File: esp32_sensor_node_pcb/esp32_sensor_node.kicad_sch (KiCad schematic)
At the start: 28 parts, among them J1 Conn_02x10_Odd_Even, Q1 2N7002K, SW1 SW_DIP_x01, SW2 SW_DIP_x01, U1 HT7833, U2 ESP32-WROOM-E, U3 MAX3483AEASA+

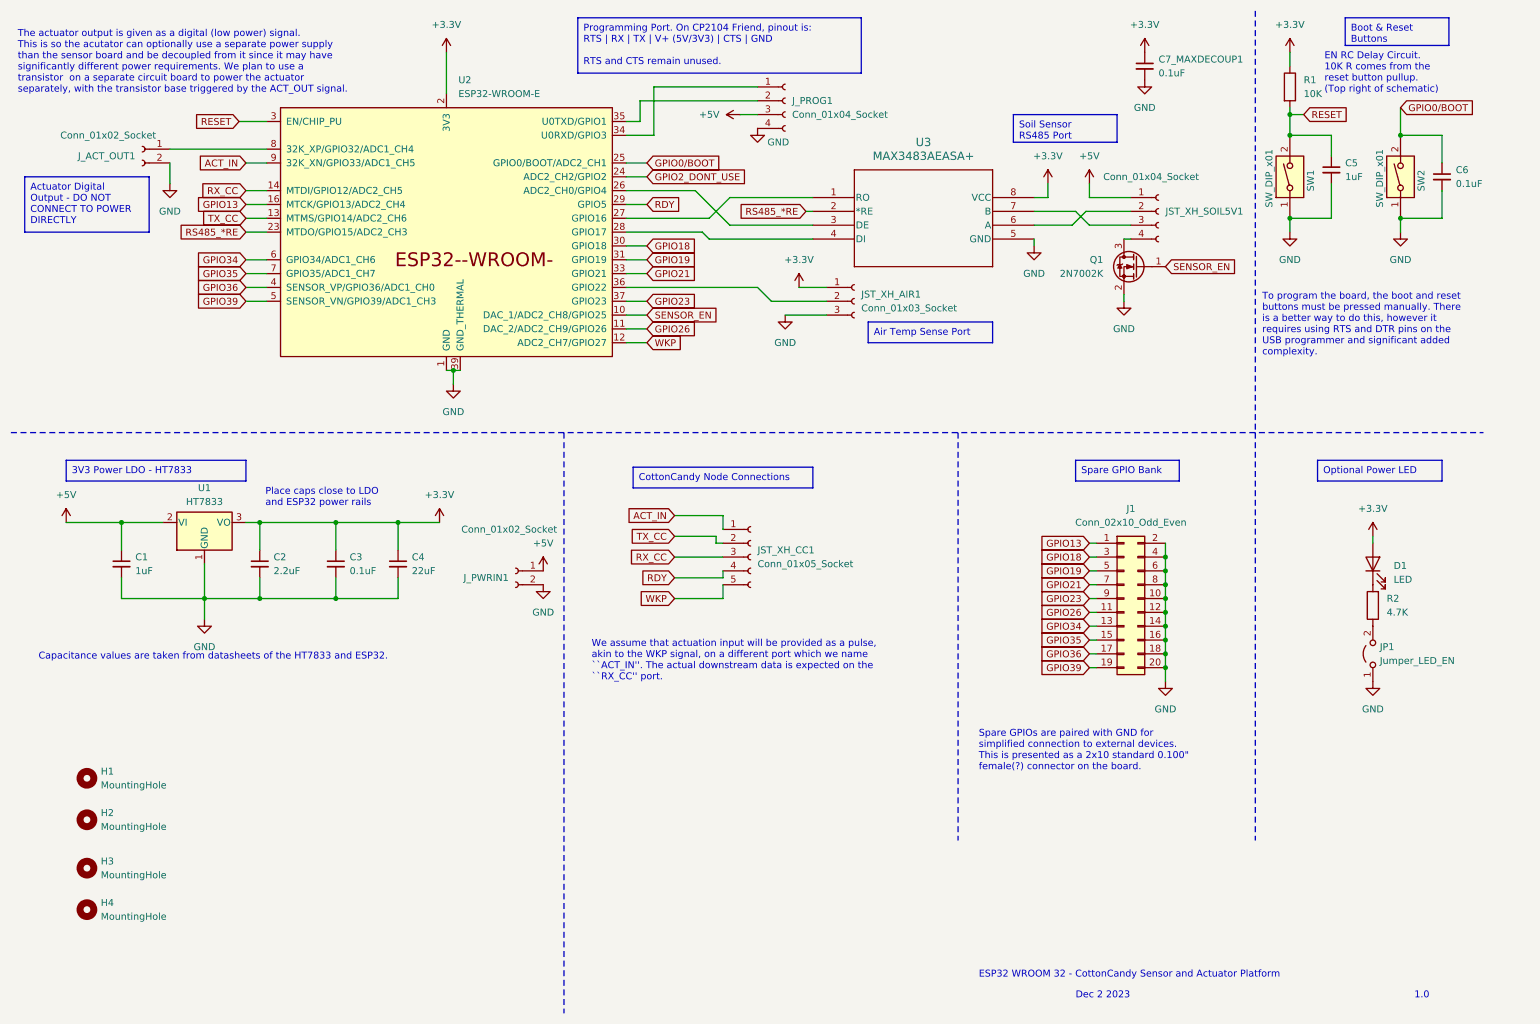
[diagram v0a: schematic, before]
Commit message: Add 3v3 outputs on header. Shift labels for alignment. Add board names on back.
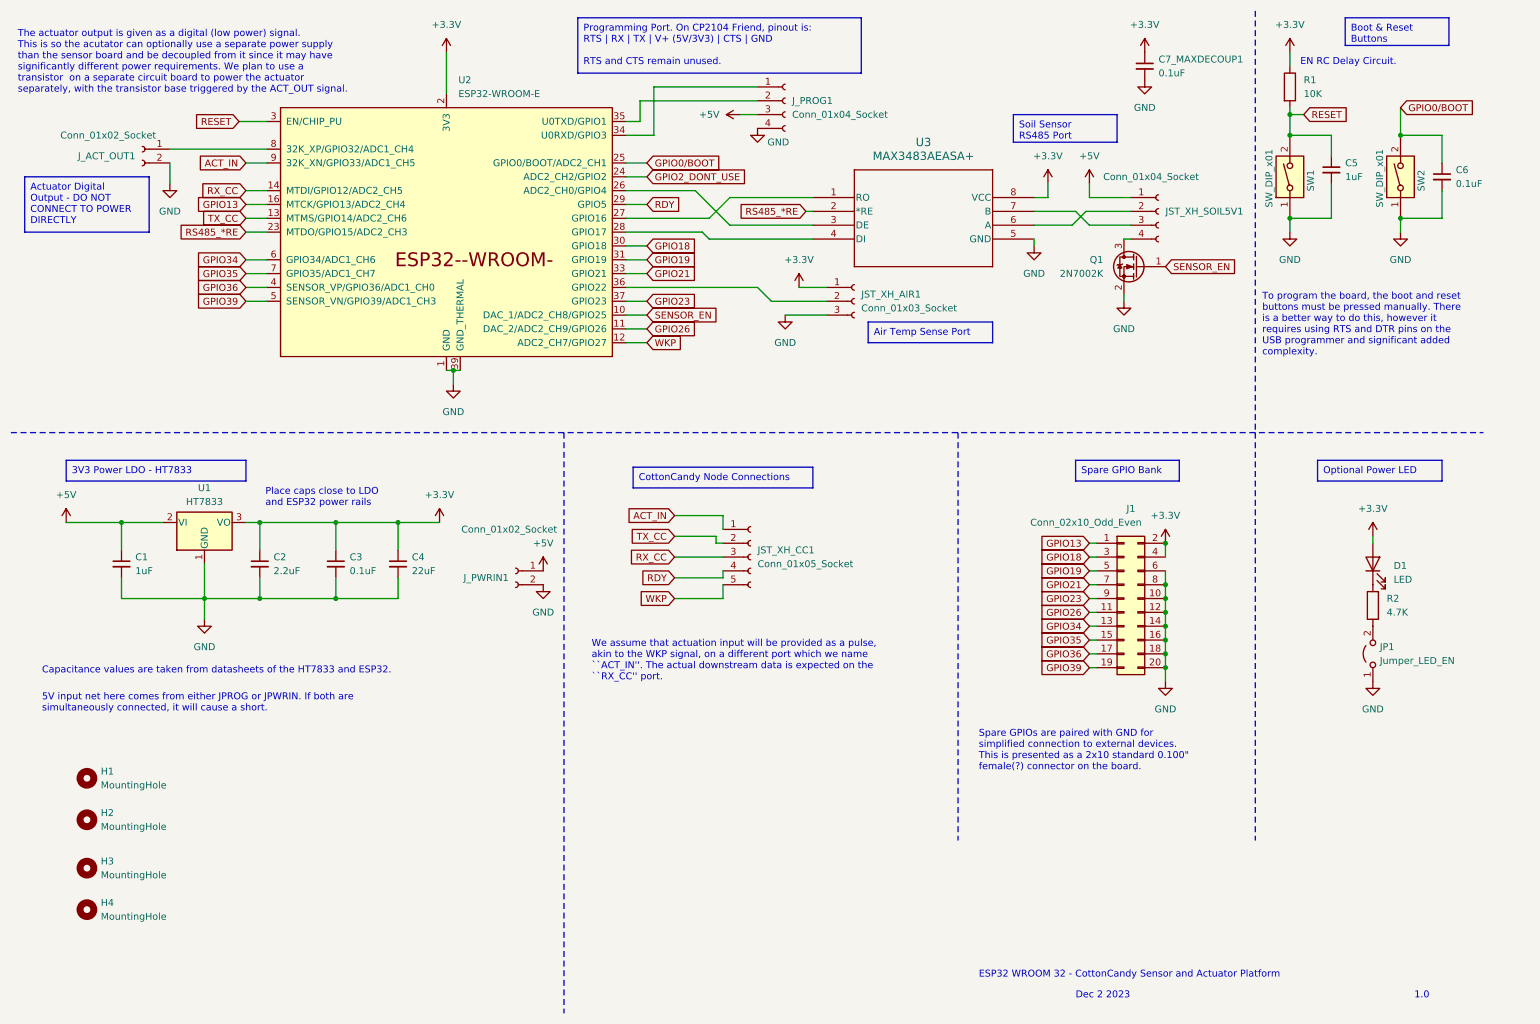
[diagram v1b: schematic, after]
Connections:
- net +3.3V: now also J1.2 (Pin_2), J1.4 (Pin_4)
- net GND: no longer J1.2 (Pin_2), J1.4 (Pin_4)
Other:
- note added: "5V input net here comes from either JPROG or JPWRIN. If both are simultaneously connected, it will cause a short."
- note added: "EN RC Delay Circuit."
- note removed: "EN RC Delay Circuit. 10K R comes from the reset button pullup. (Top right of schematic)"
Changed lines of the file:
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@@
 (kicad_sch (version 20230121) (generator eeschema)
   (paper "A4")
+  (junction (at 224.79 110.49) (diameter 0) (color 0 0 0 0)
+  )
+  (junction (at 247.65 31.75) (diameter 0) (color 0 0 0 0)
+  )
+  (junction (at 224.79 133.35) (diameter 0) (color 0 0 0 0)
+  )
+  (junction (at 83.82 106.68) (diameter 0) (color 0 0 0 0)
+  )
+  (junction (at 33.02 106.68) (diameter 0) (color 0 0 0 0)
+  )
+  (junction (at 58.42 120.65) (diameter 0) (color 0 0 0 0)
+  )
+  (junction (at 72.39 106.68) (diameter 0) (color 0 0 0 0)
+  )
+  (junction (at 224.79 128.27) (diameter 0) (color 0 0 0 0)
+  )
+  (junction (at 72.39 120.65) (diameter 0) (color 0 0 0 0)
+  )
+  (junction (at 224.79 125.73) (diameter 0) (color 0 0 0 0)
+  )
+  (junction (at 267.97 35.56) (diameter 0) (color 0 0 0 0)
+  )
+  (junction (at 224.79 120.65) (diameter 0) (color 0 0 0 0)
+  )
+  (junction (at 267.97 50.8) (diameter 0) (color 0 0 0 0)
+  )
+  (junction (at 48.26 120.65) (diameter 0) (color 0 0 0 0)
+  )
+  (junction (at 224.79 118.11) (diameter 0) (color 0 0 0 0)
+  )
+  (junction (at 247.65 35.56) (diameter 0) (color 0 0 0 0)
+  )
+  (junction (at 93.98 78.74) (diameter 0) (color 0 0 0 0)
+  )
+  (junction (at 58.42 106.68) (diameter 0) (color 0 0 0 0)
+  )
   (junction (at 224.79 123.19) (diameter 0) (color 0 0 0 0)
   )
-  (junction (at 247.65 31.75) (diameter 0) (color 0 0 0 0)
-  )
-  (junction (at 224.79 133.35) (diameter 0) (color 0 0 0 0)
-  )
-  (junction (at 83.82 106.68) (diameter 0) (color 0 0 0 0)
-  )
-  (junction (at 33.02 106.68) (diameter 0) (color 0 0 0 0)
-  )
-  (junction (at 224.79 115.57) (diameter 0) (color 0 0 0 0)
-  )
-  (junction (at 58.42 120.65) (diameter 0) (color 0 0 0 0)
-  )
-  (junction (at 72.39 106.68) (diameter 0) (color 0 0 0 0)
-  )
-  (junction (at 224.79 120.65) (diameter 0) (color 0 0 0 0)
-  )
-  (junction (at 224.79 128.27) (diameter 0) (color 0 0 0 0)
-  )
-  (junction (at 224.79 113.03) (diameter 0) (color 0 0 0 0)
-  )
-  (junction (at 72.39 120.65) (diameter 0) (color 0 0 0 0)
-  )
-  (junction (at 224.79 125.73) (diameter 0) (color 0 0 0 0)
-  )
-  (junction (at 267.97 35.56) (diameter 0) (color 0 0 0 0)
-  )
-  (junction (at 267.97 50.8) (diameter 0) (color 0 0 0 0)
-  )
-  (junction (at 48.26 120.65) (diameter 0) (color 0 0 0 0)
-  )
-  (junction (at 247.65 35.56) (diameter 0) (color 0 0 0 0)
-  )
-  (junction (at 93.98 78.74) (diameter 0) (color 0 0 0 0)
-  )
-  (junction (at 58.42 106.68) (diameter 0) (color 0 0 0 0)
-  )
-  (junction (at 224.79 118.11) (diameter 0) (color 0 0 0 0)
-  )
   (junction (at 224.79 130.81) (diameter 0) (color 0 0 0 0)
   )
@@
     (stroke (width 0) (type default))
   )
-  (wire (pts (xy 224.79 118.11) (xy 224.79 120.65))
-    (stroke (width 0) (type default))
-  )
   (wire (pts (xy 217.17 54.61) (xy 218.44 54.61))
     (stroke (width 0) (type default))
@@
     (stroke (width 0) (type default))
   )
-  (wire (pts (xy 224.79 115.57) (xy 224.79 118.11))
-    (stroke (width 0) (type default))
-  )
   (wire (pts (xy 152.4 66.04) (xy 162.56 66.04))
-    (stroke (width 0) (type default))
-  )
-  (wire (pts (xy 224.79 110.49) (xy 224.79 113.03))
     (stroke (width 0) (type default))
   )
@@
     (stroke (width 0) (type default))
   )
-  (wire (pts (xy 224.79 113.03) (xy 224.79 115.57))
-    (stroke (width 0) (type default))
-  )
   (wire (pts (xy 125.73 66.04) (xy 129.54 66.04))
     (stroke (width 0) (type default))
@@
   )
   (wire (pts (xy 255.27 44.45) (xy 255.27 50.8))
+    (stroke (width 0) (type default))
+  )
+  (wire (pts (xy 224.79 110.49) (xy 224.79 113.03))
     (stroke (width 0) (type default))
   )
@@
     (stroke (width 0) (type default))
   )
+  (wire (pts (xy 149.86 63.5) (xy 152.4 66.04))
+    (stroke (width 0) (type default))
+  )
   (wire (pts (xy 224.79 120.65) (xy 224.79 123.19))
     (stroke (width 0) (type default))
   )
-  (wire (pts (xy 149.86 63.5) (xy 152.4 66.04))
-    (stroke (width 0) (type default))
-  )
   (wire (pts (xy 140.97 54.61) (xy 160.02 54.61))
     (stroke (width 0) (type default))
@@
   )
   (wire (pts (xy 210.82 115.57) (xy 212.09 115.57))
+    (stroke (width 0) (type default))
+  )
+  (wire (pts (xy 224.79 118.11) (xy 224.79 120.65))
     (stroke (width 0) (type default))
   )
@@
   )
   (wire (pts (xy 203.2 44.45) (xy 203.2 46.99))
+    (stroke (width 0) (type default))
+  )
+  (wire (pts (xy 224.79 115.57) (xy 224.79 118.11))
     (stroke (width 0) (type default))
   )
@@
   )
   (text "Capacitance values are taken from datasheets of the HT7833 and ESP32."
-    (at 17.78 132.08 0)
+    (at 18.415 134.62 0)
     (effects (font (size 1.27 1.27)) (justify left bottom))
   )
@@
     (effects (font (size 1.27 1.27)) (justify left bottom))
   )
-  (text "EN RC Delay Circuit.\n10K R comes from the \nreset button pullup.\n(Top right of schematic)"
-    (at 254 27.94 0)
+  (text "EN RC Delay Circuit.\n" (at 249.555 22.86 0)
     (effects (font (size 1.27 1.27)) (justify left bottom))
   )
@@
   (text "ESP32 WROOM 32 - CottonCandy Sensor and Actuator Platform"
     (at 190.5 190.5 0)
+    (effects (font (size 1.27 1.27)) (justify left bottom))
+  )
+  (text "5V input net here comes from either JPROG or JPWRIN. If both are\nsimultaneously connected, it will cause a short."
+    (at 18.415 141.605 0)
     (effects (font (size 1.27 1.27)) (justify left bottom))
   )
@@
   )
   (symbol (lib_id "Connector_Generic:Conn_02x10_Odd_Even") (at 217.17 120.65 0) (unit 1)
-    (in_bom yes) (on_board yes) (dnp no) (fields_autoplaced)
+    (in_bom yes) (on_board yes) (dnp no)
     (property "Reference" "J1" (at 218.44 104.14 0)
       (effects (font (size 1.27 1.27)))
     )
-    (property "Value" "Conn_02x10_Odd_Even" (at 218.44 106.68 0)
+    (property "Value" "Conn_02x10_Odd_Even" (at 210.185 106.68 0)
       (effects (font (size 1.27 1.27)))
     )
@@
         )
       )
+    )
+  )
+  (symbol (lib_id "power:+3.3V") (at 224.79 110.49 0) (unit 1)
+    (in_bom yes) (on_board yes) (dnp no) (fields_autoplaced)
+    (property "Reference" "#PWR025" (at 224.79 114.3 0)
+      (effects (font (size 1.27 1.27)) hide)
+    )
+    (property "Value" "+3.3V" (at 224.79 105.41 0)
+      (effects (font (size 1.27 1.27)))
+    )
+    (property "Footprint" "" (at 224.79 110.49 0)
+      (effects (font (size 1.27 1.27)) hide)
+    )
+    (property "Datasheet" "" (at 224.79 110.49 0)
+      (effects (font (size 1.27 1.27)) hide)
+    )
+    (pin "1")
+    (instances
+      (project "esp32_sensor_node"
+        (path "/f305b47d-1a34-49f4-94a4-22a58fb9ed31"
+          (reference "#PWR025") (unit 1)
+        )
+      )

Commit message: Change LDO HT7833 -> SPX3819, reroute, relabel. Generate BOM testing.
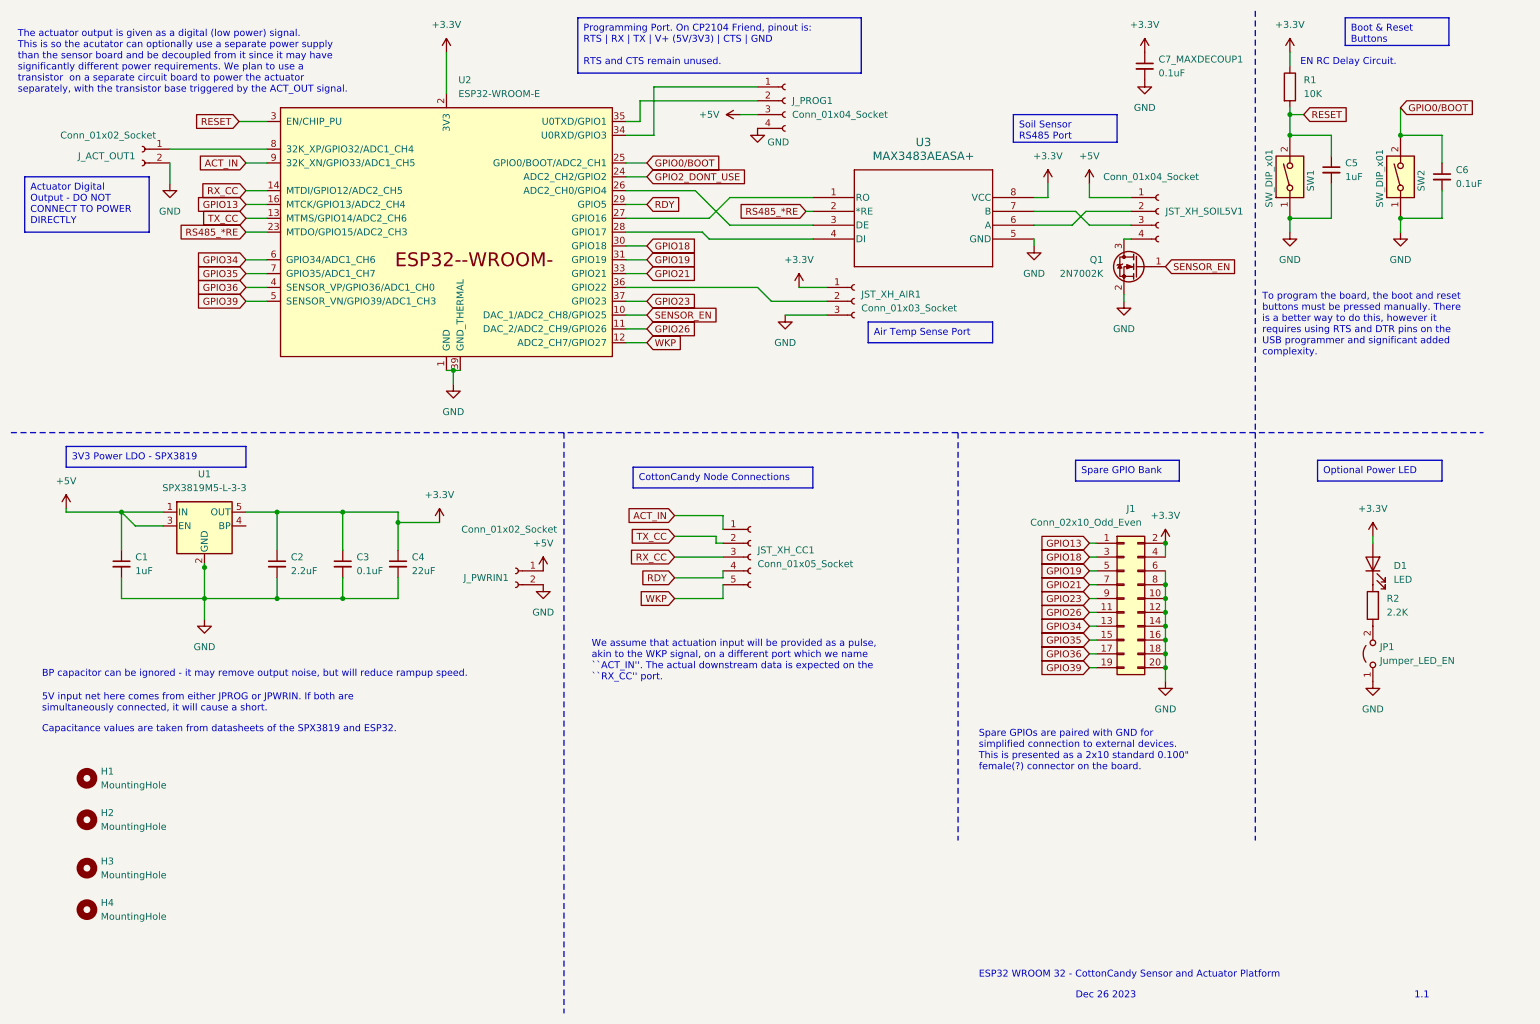
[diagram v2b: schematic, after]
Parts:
- removed U1: HT7833, Package_TO_SOT_SMD:SOT-89-3, symbol Regulator_Linear:AP2127R-3.3
- added U1: SPX3819M5-L-3-3, Package_TO_SOT_SMD:SOT-23-5, symbol Regulator_Linear:SPX3819M5-L-3-3
- R2: value 4.7K -> 2.2K
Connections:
- net +3.3V: now also U1.5 (OUT)
- net +5V: now also U1.1 (IN), U1.3 (EN)
- net GND: now also U1.2 (GND)
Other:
- note added: "1.1"
- note added: "BP capacitor can be ignored - it may remove output noise, but will reduce rampup speed."
- note added: "Capacitance values are taken from datasheets of the SPX3819 and ESP32."
- note added: "Dec 26 2023"
- note removed: "1.0"
- note removed: "Capacitance values are taken from datasheets of the HT7833 and ESP32."
- note removed: "Dec 2 2023"
- moved on the sheet: C2, C3

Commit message: Changed 2.2uF cap to 0805. Added power flag on 5V and not-connected for BP pin. Changed all vias to 0.3mm hole size. Changed programming interface to 2.54mm PIN headers.
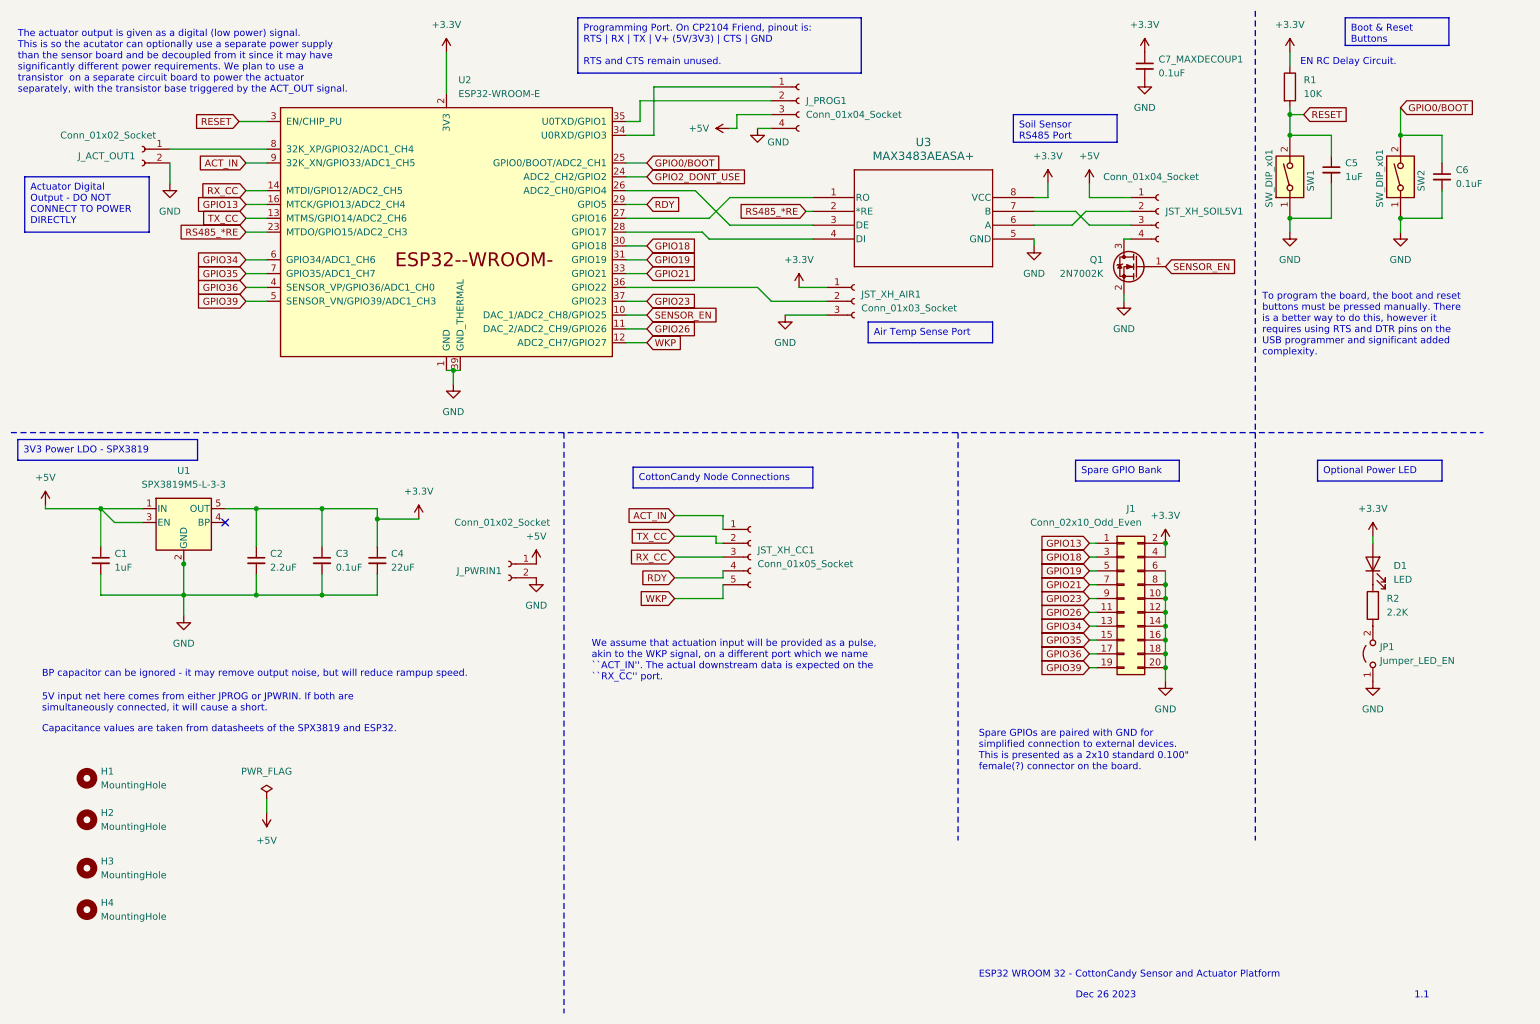
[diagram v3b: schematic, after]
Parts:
- C2: footprint Capacitor_SMD:C_0603_1608Metric -> Capacitor_SMD:C_0805_2012Metric
- J_PROG1: footprint Connector_JST:JST_XH_B4B-XH-A_1x04_P2.50mm_Vertical -> Connector_PinSocket_2.54mm:PinSocket_1x04_P2.54mm_Vertical
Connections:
- no-connect marks 0 -> 1
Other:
- moved on the sheet: C1, C2, C3, C4, J_PWRIN1, U1
